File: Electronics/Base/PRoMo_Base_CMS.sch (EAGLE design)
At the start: 17 parts, among them IC1 DSPIC33FJ128MC804-PT, IC2 LM1117IMPX-3.3, X1 PN61729-S

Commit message: Avancement de la carte de base
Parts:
- added C5: 10µF, resistor:C-EUC1206
- added C6, C7, C8, C9: 100nF, resistor:C-EUC1206
- added IC3: FT232RL, ftdichip-3:FT232RL
- added JP2: PICKit, pinhead:PINHD-1X6/90
- added LED3, LED4: (no value), led:LEDCHIPLED_1206
- added R2: 353, resistor:R-EU_M1206
- added RLED3, RLED4: 56, resistor:R-EU_M1206
- added S1: (no value), switch-omron:10-XX
- J1: value (none) -> CON Jack
- P1: value (none) -> Bornier
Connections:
- new net !MCLR!: IC1.MCLR, JP2.1, R2.1, S1.S, S1.S1
- new net N$10: LED3.A, RLED3.2
- new net N$11: LED4.A, RLED4.2
- new net N$12: IC3.CBUS1, LED4.C
- new net N$13: C9.2, IC3.3V3OUT
- new net N$6: IC3.TXD
- new net N$8: IC3.RXD
- new net N$9: IC3.CBUS0, LED3.C
- new net PGEC: IC1.PGEC1/AN3/C2IN+/RP1/CN5/RB1, JP2.5
- new net PGED: IC1.PGED1/AN2/C2IN-/RP0/CN4/RB0, JP2.4
- new net VCAP: C5.1, IC1.VCAP/VDDCORE
- net +3V3: now also C6.1, C7.1, C8.1, IC1.AVDD, IC1.VDD, IC1.VDD1, IC3.VCCIO, JP2.2, R2.2, RLED3.1, RLED4.1
- net +5V: now also IC3.VCC
- net D+: now also IC3.USBDP
- net D-: now also IC3.USBDM
- net PE: now also C5.2, C6.2, C7.2, C8.2, C9.1, IC1.AVSS, IC1.VSS, IC1.VSS2, IC3.AGND, IC3.GND1, IC3.GND2, IC3.GND3, IC3.TEST, JP2.3, S1.P, S1.P1
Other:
- note added: "Capas de découplage : A mettre au plus près du PIC"
- moved on the sheet: C3, C4, IC2, JP1, LED2, RLED2

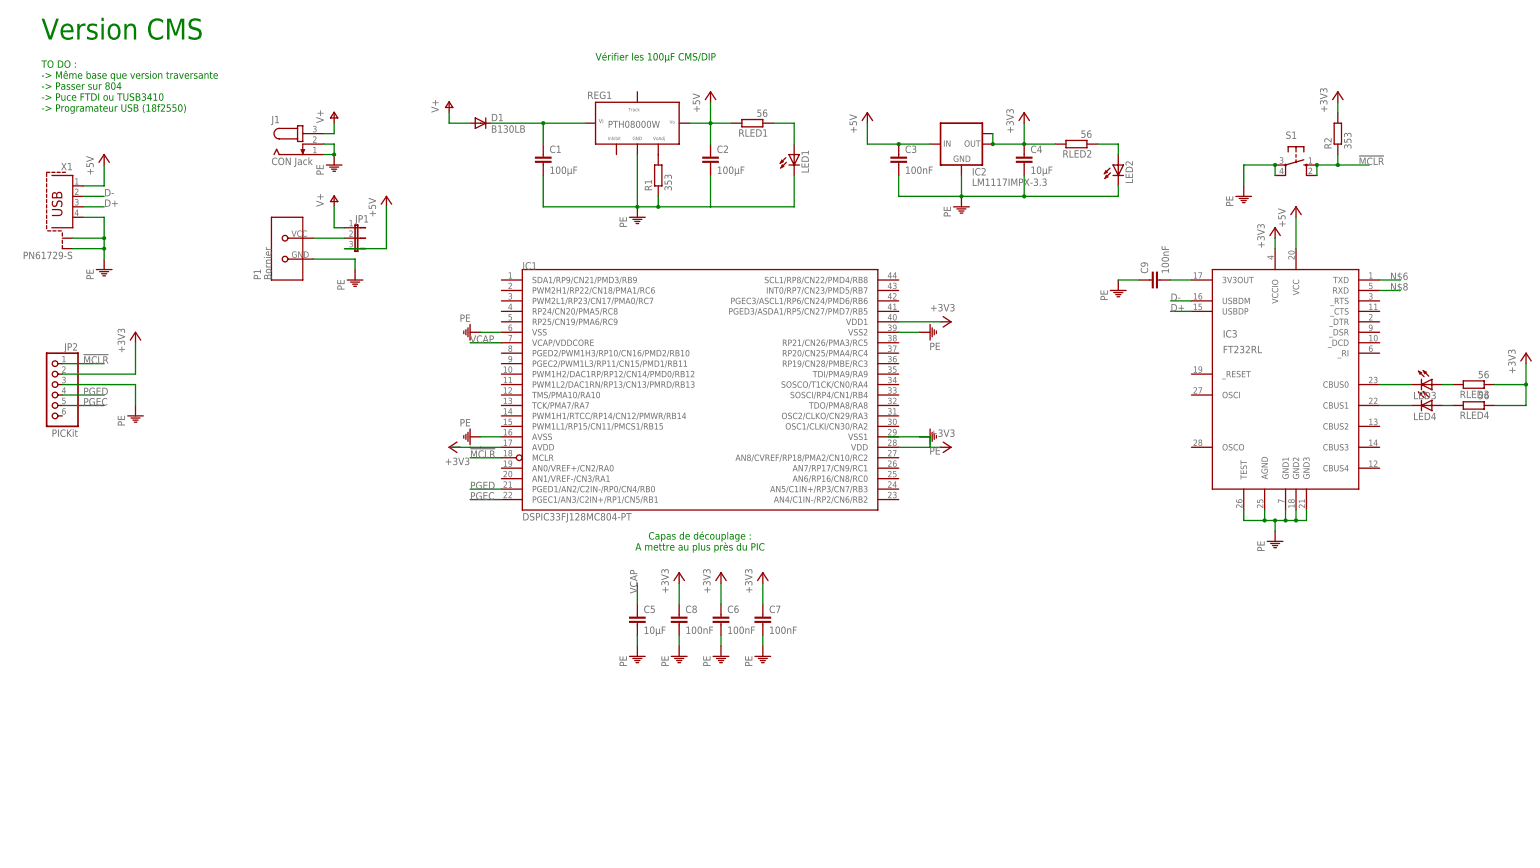
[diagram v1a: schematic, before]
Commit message: Choix des pins et début du routage
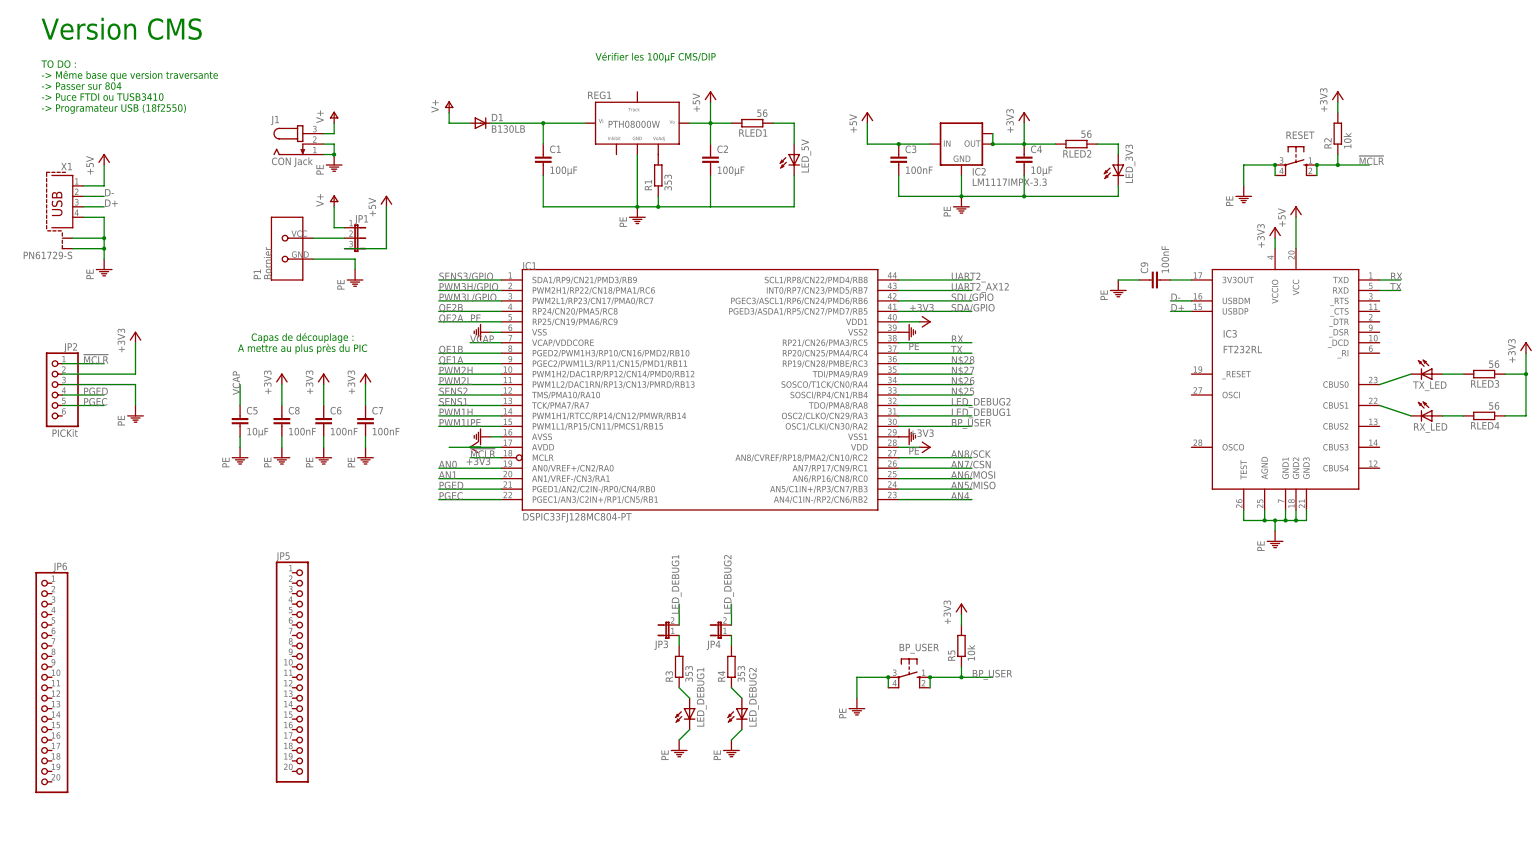
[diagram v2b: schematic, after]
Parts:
- removed LED3, LED4: (no value), led:LEDCHIPLED_1206
- added BP_USER: (no value), switch-omron:10-XX
- added JP3, JP4: (no value), jumper:JP1E
- added JP5, JP6: (no value), pinhead:PINHD-1X20
- added LED_DEBUG1, LED_DEBUG2, RX_LED, TX_LED: (no value), led:LEDCHIPLED_1206
- added R3, R4: 353, resistor:R-EU_M1206
- added R5: 10k, resistor:R-EU_M1206
- R2: value 353 -> 10k
- renumbered LED1 to LED_5V, LED2 to LED_3V3, S1 to RESET
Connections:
- removed net N$6: IC3.TXD
- removed net N$8: IC3.RXD
- new net AN0: IC1.AN0/VREF+/CN2/RA0
- new net AN1: IC1.AN1/VREF-/CN3/RA1
- new net AN4: IC1.AN4/C1IN-/RP2/CN6/RB2
- new net AN5/MISO: IC1.AN5/C1IN+/RP3/CN7/RB3
- new net AN6/MOSI: IC1.AN6/RP16/CN8/RC0
- new net AN7/CSN: IC1.AN7/RP17/CN9/RC1
- new net AN8/SCK: IC1.AN8/CVREF/RP18/PMA2/CN10/RC2
- new net BP_USER: BP_USER.S, BP_USER.S1, IC1.OSC1/CLKI/CN30/RA2, R5.1
- new net LED_DEBUG1: IC1.OSC2/CLKO/CN29/RA3, JP3.2
- new net LED_DEBUG2: IC1.TDO/PMA8/RA8, JP4.2
- new net N$14: LED_DEBUG2.A, R4.1
- new net N$15: JP3.1, R3.2
- new net N$16: JP4.1, R4.2
- new net N$25: IC1.SOSCI/RP4/CN1/RB4
- new net N$26: IC1.SOSCO/T1CK/CN0/RA4
- new net N$27: IC1.TDI/PMA9/RA9
- new net N$28: IC1.RP19/CN28/PMBE/RC3
- new net N$5: LED_DEBUG1.A, R3.1
- new net PWM1H: IC1.PWM1H1/RTCC/RP14/CN12/PMWR/RB14
- new net PWM1L: IC1.PWM1L1/RP15/CN11/PMCS1/RB15
- new net PWM2H: IC1.PWM1H2/DAC1RP/RP12/CN14/PMD0/RB12
- new net PWM2L: IC1.PWM1L2/DAC1RN/RP13/CN13/PMRD/RB13
- new net PWM3H/GPIO: IC1.PWM2H1/RP22/CN18/PMA1/RC6
- new net PWM3L/GPIO: IC1.PWM2L1/RP23/CN17/PMA0/RC7
- new net QE1A: IC1.PGEC2/PWM1L3/RP11/CN15/PMD1/RB11
- new net QE1B: IC1.PGED2/PWM1H3/RP10/CN16/PMD2/RB10
- new net QE2A: IC1.RP25/CN19/PMA6/RC9
- new net QE2B: IC1.RP24/CN20/PMA5/RC8
- new net RX: IC1.RP21/CN26/PMA3/RC5, IC3.TXD
- new net SDA/GPIO: IC1.PGED3/ASDA1/RP5/CN27/PMD7/RB5
- new net SDL/GPIO: IC1.PGEC3/ASCL1/RP6/CN24/PMD6/RB6
- new net SENS1: IC1.TCK/PMA7/RA7
- new net SENS2: IC1.TMS/PMA10/RA10
- new net SENS3/GPIO: IC1.SDA1/RP9/CN21/PMD3/RB9
- new net TX: IC1.RP20/CN25/PMA4/RC4, IC3.RXD
- new net UART2_: IC1.SCL1/RP8/CN22/PMD4/RB8
- new net UART2_AX12: IC1.INT0/RP7/CN23/PMD5/RB7
- net +3V3: now also R5.2
- net N$10: now also TX_LED.A; no longer LED3.A
- net N$11: now also RX_LED.A; no longer LED4.A
- net N$12: now also RX_LED.C; no longer LED4.C
- net N$9: now also TX_LED.C; no longer LED3.C
- net PE: now also BP_USER.P, BP_USER.P1, IC1.VSS1, LED_DEBUG1.C, LED_DEBUG2.C
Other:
- moved on the sheet: C5, C6, C7, C8, RLED3, RLED4

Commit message: Utilisation Lib SeeedStudio
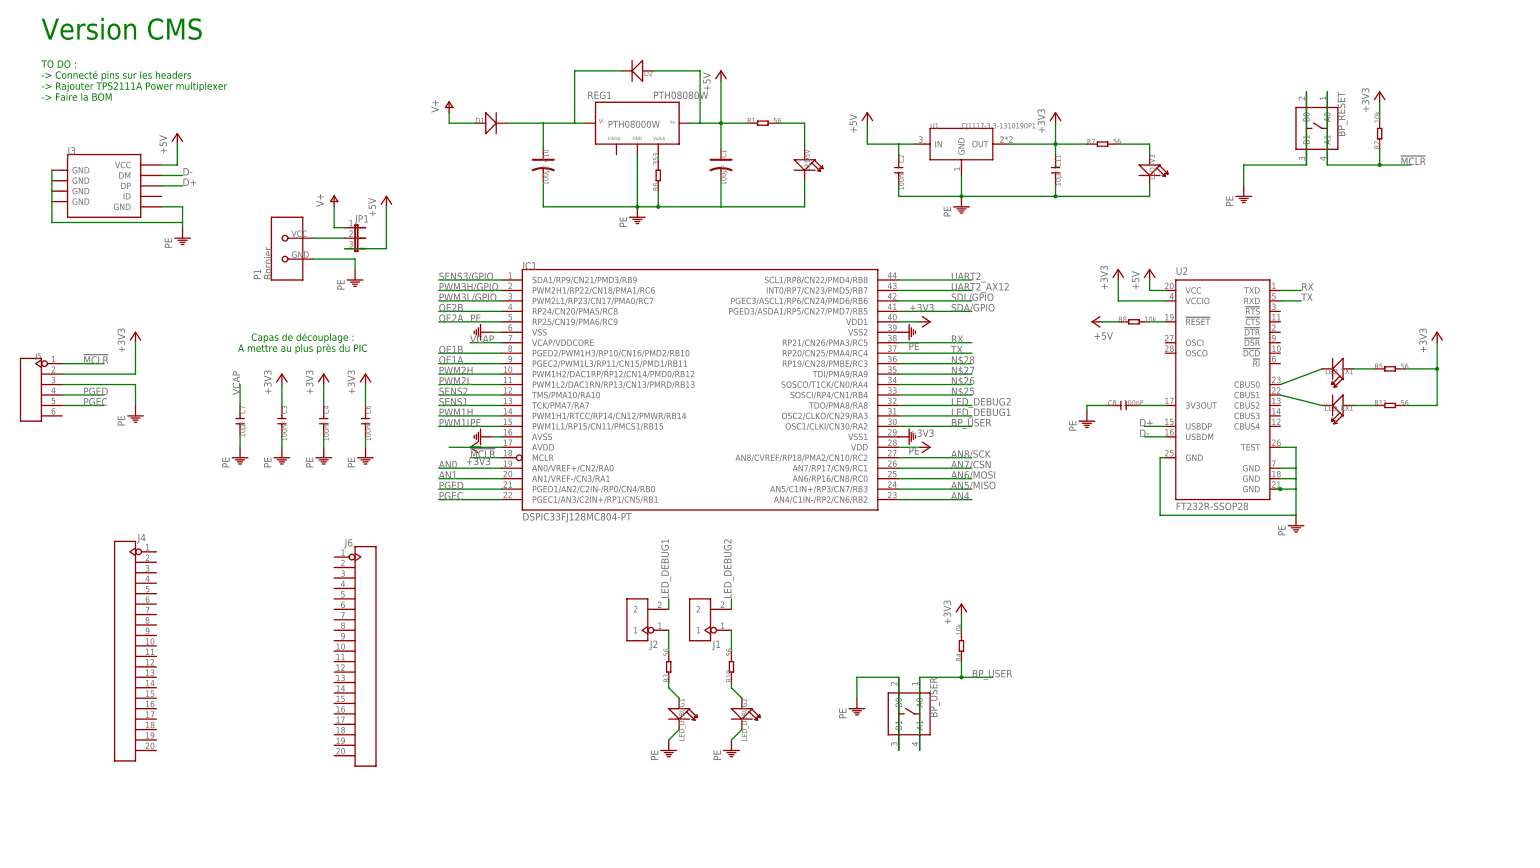
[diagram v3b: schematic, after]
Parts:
- removed C5: 10µF, resistor:C-EUC1206
- removed C9: 100nF, resistor:C-EUC1206
- removed IC2: LM1117IMPX-3.3, lm1117:LM1117IMPX-3.3
- removed IC3: FT232RL, ftdichip-3:FT232RL
- removed JP2: PICKit, pinhead:PINHD-1X6/90
- removed JP3, JP4: (no value), jumper:JP1E
- removed JP5, JP6: (no value), pinhead:PINHD-1X20
- removed LED_3V3, LED_5V, RX_LED, TX_LED: (no value), led:LEDCHIPLED_1206
- removed RESET: (no value), switch-omron:10-XX
- removed RLED1, RLED2, RLED3, RLED4: 56, resistor:R-EU_M1206
- removed X1: PN61729-S, con-berg:PN61729-S
- added BP_RESET: (no value), Discrete:BUTTON-4P-6.2X6.2
- added C10: 100µF, Discrete:CAP-D5.3/2.0
- added C11: 10µF, Discrete:C-1206
- added D2: (no value), Discrete:D'DO-214AB'
- added J2: (no value), Connector :HEADER-2P-65/35MIL
- added J3: (no value), Connector :USB-MINIUSB-5P-TH
- added J4, J6: (no value), Connector :HEADER-20P-2.54
- added J5: (no value), Connector :HEADER-6P-60/35MIL
- added LED3V3, LED5V, LED_RX1, LED_TX1: (no value), Discrete:LED'1206'
- added R10, R11, R7: 56, Discrete:R-1206
- added R6: 353, Discrete:R-0204/7
- added R8: 10k, Discrete:R-1206
- added U1: CJ1117-3.3-1310190P1, OPL:CJ1117-3.3-1310190P1
- added U2: FT232R-SSOP28, IC:FT232R-SSOP28
- BP_USER: device switch-omron:10-XX -> Discrete:BUTTON-4P-6.2X6.2
- C1: device resistor:C-EUC1206 -> Discrete:CAP-D5.3/2.0
- C2: value 100µF -> 100nF; device resistor:C-EUC1206 -> Discrete:C-1206
- C3, C6, C8: device resistor:C-EUC1206 -> Discrete:C-1206
- C4: value 10µF -> 100nF; device resistor:C-EUC1206 -> Discrete:C-1206
- C7: value 100nF -> 10µF; device resistor:C-EUC1206 -> Discrete:C-1206
- D1: value B130LB -> (none); device diode:DIODE-SMB -> Discrete:D'DO-214AB'
- J1: value CON Jack -> (none); device con-jack:JACK-PLUG1 -> Connector :HEADER-2P-65/35MIL
- LED_DEBUG1, LED_DEBUG2: device led:LEDCHIPLED_1206 -> Discrete:LED'1206'
- R1, R3: value 353 -> 56; device resistor:R-EU_M1206 -> Discrete:R-1206
- R2: device resistor:R-EU_M1206 -> Discrete:R-1206
- R4: value 353 -> 10k; device resistor:R-EU_M1206 -> Discrete:R-1206
- R5: value 10k -> 56; device resistor:R-EU_M1206 -> Discrete:R-1206
- REG1: value (none) -> PTH08080W; device Perso:PTH08000W(EUS) -> Perso:PTH08080W
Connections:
- removed net N$10: RLED3.2, TX_LED.A
- removed net N$11: RLED4.2, RX_LED.A
- removed net N$12: IC3.CBUS1, RX_LED.C
- removed net N$13: C9.2, IC3.3V3OUT
- new net N$17: LED_TX1.+, R5.1
- new net N$18: LED_RX1.+, R11.1
- new net N$19: LED_RX1.-, U2.CBUS1
- new net N$6: J2.1, R3.2
- new net N$8: C8.2, U2.3V3OUT
- net !MCLR!: now also BP_RESET.A0, BP_RESET.A1, J5.1; no longer JP2.1, RESET.S, RESET.S1
- net +3V3: now also C11.1, C3.1, J5.2, R11.2, R4.2, R7.1, U1.OUT, U2.VCCIO; no longer C7.1, C8.1, IC2.OUT, IC2.OUT1, IC3.VCCIO, JP2.2, RLED2.2, RLED3.1, RLED4.1
- net +5V: now also C1.+, D2.+, J3.VCC, R1.1, R8.1, REG1.5_VO, U1.IN, U2.VCC; no longer C3.1, IC2.IN, IC3.VCC, REG1.6, RLED1.2, X1.1
- net BP_USER: now also BP_USER.A0, BP_USER.A1, R4.1; no longer BP_USER.S, BP_USER.S1, R5.1
- net D+: now also J3.DP, U2.USBDP; no longer IC3.USBDP, X1.3
- net D-: now also J3.DM, U2.USBDM; no longer IC3.USBDM, X1.2
- net LED_DEBUG1: now also J2.2; no longer JP3.2
- net LED_DEBUG2: now also J1.2; no longer JP4.2
- net N$1: now also C10.+, D1.-, D2.-, REG1.1_VI; no longer C1.1, D1.C, REG1.3
- net N$14: now also LED_DEBUG2.+, R10.1; no longer LED_DEBUG2.A, R4.1
- net N$15: now also LED_TX1.-, U2.CBUS0; no longer JP3.1, R3.2
- net N$16: now also J1.1, R10.2; no longer JP4.1, R4.2
- net N$2: now also R6.2, REG1.4_VOADJ; no longer R1.2, REG1.5
- net N$3: now also LED5V.+, R1.2; no longer LED_5V.A, RLED1.1
- net N$5: now also LED_DEBUG1.+; no longer LED_DEBUG1.A
- net N$7: now also LED3V3.+, R7.2; no longer LED_3V3.A, RLED2.1
- net N$9: now also R8.2, U2.!RESET; no longer IC3.CBUS0, TX_LED.C
- net PE: now also BP_RESET.B0, BP_RESET.B1, BP_USER.B0, BP_USER.B1, C1.-, C10.-, C11.2, C8.1, J3.GND@1, J3.GND@2, J3.GND@3, J3.GND@4, J3.GND@5, J5.3, LED3V3.-, LED5V.-, LED_DEBUG1.-, LED_DEBUG2.-, R6.1, REG1.3_GND, U1.GND, U2.GND, U2.GND@1, U2.GND@2, U2.GND@A, U2.TEST; no longer BP_USER.P, BP_USER.P1, C1.2, C5.2, C8.2, C9.1, IC2.GND, IC3.AGND, IC3.GND1, IC3.GND2, IC3.GND3, IC3.TEST, J1.1, J1.2, JP2.3, LED_3V3.C, LED_5V.C, LED_DEBUG1.C, LED_DEBUG2.C, R1.1, REG1.1, RESET.P, RESET.P1, X1.4, X1.S1, X1.S2
- net PGEC: now also J5.5; no longer JP2.5
- net PGED: now also J5.4; no longer JP2.4
- net RX: now also U2.TXD; no longer IC3.TXD
- net TX: now also U2.RXD; no longer IC3.RXD
- net V+: now also D1.+; no longer D1.A, J1.3
- net VCAP: now also C7.1; no longer C5.1
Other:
- note added: "TO DO : -> Connecté pins sur les headers -> Rajouter TPS2111A Power multiplexer -> Faire la BOM"
- note removed: "TO DO : -> Même base que version traversante -> Passer sur 804 -> Puce FTDI ou TUSB3410 -> Programateur USB (18f2550)"
- note removed: "Vérifier les 100µF CMS/DIP"

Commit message: Schématique OK, début routage
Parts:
- removed J1, J2: (no value), Connector :HEADER-2P-65/35MIL
- removed J4, J6: (no value), Connector :HEADER-20P-2.54
- removed J5: (no value), Connector :HEADER-6P-60/35MIL
- added JP2: (no value), pinhead:PINHD-1X22
- added JP3: (no value), jumper:JP2Q
- added JP4: (no value), pinhead:PINHD-1X6/90
- added JP5: (no value), jumper:JP3Q
- added Q1: (no value), Discrete:MOSFET-P'SI2323CDS/SI2305DS<BR>'
- added R12, R23, R24, R9: (no value), Discrete:R-0805
- C11, C2, C3, C4, C6, C7, C8: device Discrete:C-1206 -> Discrete:C-0805
- D1, D2: device Discrete:D'DO-214AB' -> Discrete:D'1206'
- JP1: device jumper:JP2E -> pinhead:PINHD-1X22
- R1, R10, R11, R2, R3, R4, R5, R7, R8: device Discrete:R-1206 -> Discrete:R-0805
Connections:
- removed net AN0: IC1.AN0/VREF+/CN2/RA0
- removed net AN1: IC1.AN1/VREF-/CN3/RA1
- removed net AN4: IC1.AN4/C1IN-/RP2/CN6/RB2
- removed net AN5/MISO: IC1.AN5/C1IN+/RP3/CN7/RB3
- removed net AN6/MOSI: IC1.AN6/RP16/CN8/RC0
- removed net AN7/CSN: IC1.AN7/RP17/CN9/RC1
- removed net AN8/SCK: IC1.AN8/CVREF/RP18/PMA2/CN10/RC2
- removed net BP_USER: BP_USER.A0, BP_USER.A1, IC1.OSC1/CLKI/CN30/RA2, R4.1
- removed net LED_DEBUG1: IC1.OSC2/CLKO/CN29/RA3, J2.2
- removed net LED_DEBUG2: IC1.TDO/PMA8/RA8, J1.2
- removed net N$1: C10.+, D1.-, D2.-, REG1.1_VI
- removed net N$18: LED_RX1.+, R11.1
- removed net N$19: LED_RX1.-, U2.CBUS1
- removed net N$25: IC1.SOSCI/RP4/CN1/RB4
- removed net N$26: IC1.SOSCO/T1CK/CN0/RA4
- removed net N$27: IC1.TDI/PMA9/RA9
- removed net N$28: IC1.RP19/CN28/PMBE/RC3
- removed net N$4: JP1.2, P1.VCC
- removed net PWM1H: IC1.PWM1H1/RTCC/RP14/CN12/PMWR/RB14
- removed net PWM1L: IC1.PWM1L1/RP15/CN11/PMCS1/RB15
- removed net PWM2H: IC1.PWM1H2/DAC1RP/RP12/CN14/PMD0/RB12
- removed net PWM2L: IC1.PWM1L2/DAC1RN/RP13/CN13/PMRD/RB13
- removed net PWM3H/GPIO: IC1.PWM2H1/RP22/CN18/PMA1/RC6
- removed net PWM3L/GPIO: IC1.PWM2L1/RP23/CN17/PMA0/RC7
- removed net QE1A: IC1.PGEC2/PWM1L3/RP11/CN15/PMD1/RB11
- removed net QE1B: IC1.PGED2/PWM1H3/RP10/CN16/PMD2/RB10
- removed net QE2A: IC1.RP25/CN19/PMA6/RC9
- removed net QE2B: IC1.RP24/CN20/PMA5/RC8
- removed net RX: IC1.RP21/CN26/PMA3/RC5, U2.TXD
- removed net SDA/GPIO: IC1.PGED3/ASDA1/RP5/CN27/PMD7/RB5
- removed net SDL/GPIO: IC1.PGEC3/ASCL1/RP6/CN24/PMD6/RB6
- removed net SENS1: IC1.TCK/PMA7/RA7
- removed net SENS2: IC1.TMS/PMA10/RA10
- removed net SENS3/GPIO: IC1.SDA1/RP9/CN21/PMD3/RB9
- removed net TX: IC1.RP20/CN25/PMA4/RC4, U2.RXD
- removed net UART2_: IC1.SCL1/RP8/CN22/PMD4/RB8
- removed net UART2_AX12: IC1.INT0/RP7/CN23/PMD5/RB7
- new net AN0/RA0: IC1.AN0/VREF+/CN2/RA0, JP3.1, R12.2, R9.2
- new net AN1/RA1: IC1.AN1/VREF-/CN3/RA1, JP3.3, R23.2, R24.2
- new net AN4/RP2/RB2: IC1.AN4/C1IN-/RP2/CN6/RB2, JP2.18
- new net AN5/MISO/RP3/RB3: IC1.AN5/C1IN+/RP3/CN7/RB3, JP2.19
- new net AN6/MOSI/RP16/RC0: IC1.AN6/RP16/CN8/RC0, JP2.20
- new net AN7/CSN/RP17/RC1: IC1.AN7/RP17/CN9/RC1, JP2.21
- new net AN8/SCK/RP18/RC2: IC1.AN8/CVREF/RP18/PMA2/CN10/RC2, JP2.22
- new net BP: BP_USER.A0, BP_USER.A1, JP5.5, R4.1
- new net BP_USER/RA8: IC1.TDO/PMA8/RA8, JP1.20, JP5.6
- new net LED_DEBUG1/RA2: IC1.OSC1/CLKI/CN30/RA2, JP1.22
- new net LED_DEBUG2/RA3: IC1.OSC2/CLKO/CN29/RA3, JP1.21, JP5.4
- new net N$10: JP2.17, JP3.4, R23.1
- new net N$11: JP2.16, JP3.2, R9.1
- new net N$12: R11.1, U2.CBUS1
- new net N$13: R5.1, U2.CBUS0
- new net PWM1H/RP14/RB14: IC1.PWM1H1/RTCC/RP14/CN12/PMWR/RB14, JP2.14
- new net PWM1L/RP14/RB15: IC1.PWM1L1/RP15/CN11/PMCS1/RB15, JP2.15
- new net PWM2H/RP12/RB12: IC1.PWM1H2/DAC1RP/RP12/CN14/PMD0/RB12, JP2.10
- new net PWM2L/RP13/RB13: IC1.PWM1L2/DAC1RN/RP13/CN13/PMRD/RB13, JP2.11
- new net PWM3H/RP22: IC1.PWM2H1/RP22/CN18/PMA1/RC6, JP1.8
- new net PWM3L/RP23: IC1.PWM2L1/RP23/CN17/PMA0/RC7, JP1.7
- new net QE1A/RP11/RB11: IC1.PGEC2/PWM1L3/RP11/CN15/PMD1/RB11, JP2.9
- new net QE1B/RP10/RB10: IC1.PGED2/PWM1H3/RP10/CN16/PMD2/RB10, JP2.8
- new net QE2A/RP25/RC9: IC1.RP25/CN19/PMA6/RC9, JP2.7
- new net QE2B/RP24/RC8: IC1.RP24/CN20/PMA5/RC8, JP2.6
- new net RA4: IC1.SOSCO/T1CK/CN0/RA4, JP1.18
- new net RA9: IC1.TDI/PMA9/RA9, JP1.17
- new net RP21/RC5: IC1.RP21/CN26/PMA3/RC5, JP1.14
- new net RP4/RB4: IC1.SOSCI/RP4/CN1/RB4, JP1.19
- new net RX_FTDI: IC1.INT0/RP7/CN23/PMD5/RB7, JP1.10, U2.TXD
- new net SDA/RP5/RB5: IC1.PGED3/ASDA1/RP5/CN27/PMD7/RB5, JP1.13
- new net SDL/RP6/RB6: IC1.PGEC3/ASCL1/RP6/CN24/PMD6/RB6, JP1.12
- new net SENS1/RA7: IC1.TCK/PMA7/RA7, JP2.13
- new net SENS2/RA10: IC1.TMS/PMA10/RA10, JP2.12
- new net SENS3/RP9/RB9: IC1.SDA1/RP9/CN21/PMD3/RB9, JP1.9
- new net TX_FTDI: IC1.SCL1/RP8/CN22/PMD4/RB8, JP1.11, U2.RXD
- new net UART_AX12/RP19/RC3: IC1.RP19/CN28/PMBE/RC3, JP1.16
- new net UART_BIS/RP20/RC4: IC1.RP20/CN25/PMA4/RC4, JP1.15
- new net VIN: C10.+, D1.-, D2.-, JP2.1, JP2.2, Q1.G, REG1.1_VI
- new net VUSB: J3.VCC, Q1.D
- net !MCLR!: now also JP4.6; no longer J5.1
- net +3V3: now also JP1.3, JP1.4, JP4.5, LED_RX1.+, LED_TX1.+; no longer J5.2, R11.2, R5.2
- net +5V: now also JP1.1, JP1.2, Q1.S, REG1.3_VO; no longer J3.VCC, JP1.3, REG1.5_VO
- net N$15: now also R5.2; no longer U2.CBUS0
- net N$16: now also JP5.3; no longer J1.1
- net N$17: now also LED_RX1.-, R11.2; no longer LED_TX1.+, R5.1
- net N$6: now also JP5.1; no longer J2.1
- net PE: now also JP1.5, JP1.6, JP2.3, JP2.4, JP2.5, JP4.4, R12.1, R24.1, REG1.2_GND; no longer J5.3, REG1.3_GND
- net PGEC: now also JP4.2; no longer J5.5
- net PGED: now also JP4.3; no longer J5.4
- net V+: now also P1.VCC; no longer JP1.1
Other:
- note added: "TO DO : -> Mettre les empreintes (Jumpers) pour les ponts diviseurs (ANs) -> Faire la BOM"
- note removed: "TO DO : -> Connecté pins sur les headers -> Rajouter TPS2111A Power multiplexer -> Faire la BOM"
- moved on the sheet: BP_USER, C3, C4, C6, C7, IC1, J3, LED_DEBUG1, LED_DEBUG2, LED_RX1, LED_TX1, P1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
